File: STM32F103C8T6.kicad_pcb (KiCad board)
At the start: 2 copper layers, 28 parts, among them J1 USB_B_Micro, J2 Conn_01x04_Pin, J3 Conn_01x04_Pin, J4 Conn_01x04_Pin, SW1 SW_SPDT, U1 STM32F103C8T6, U3 AMS1117-3.3, Y1 16MHz

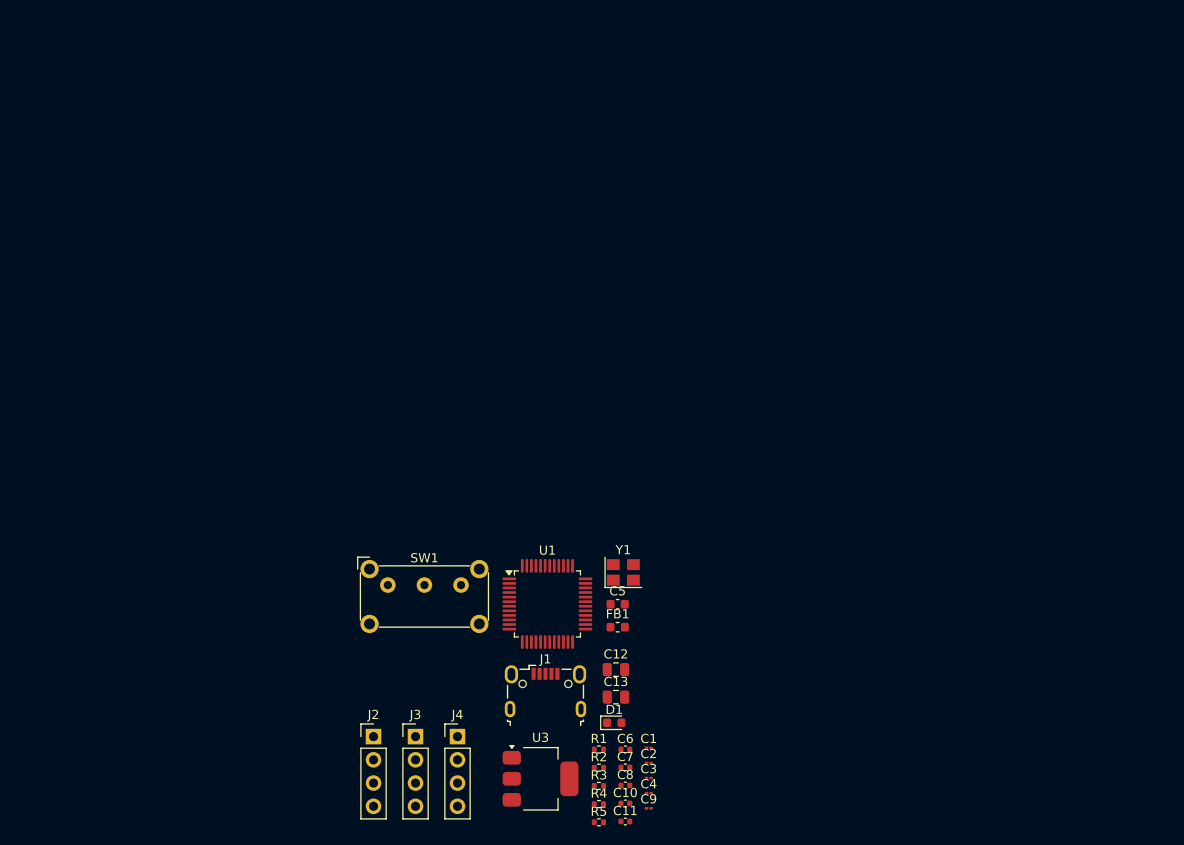
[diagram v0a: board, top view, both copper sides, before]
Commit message: footprint corrected, layout started
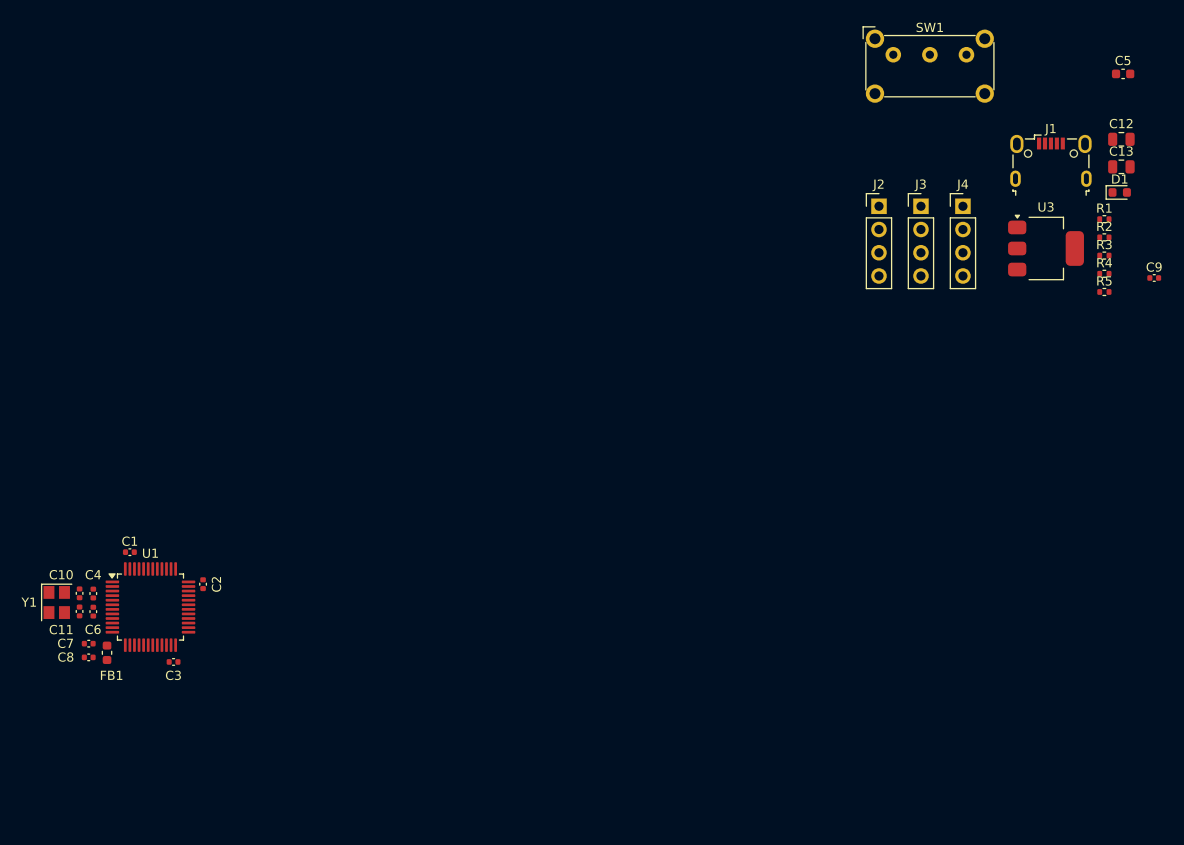
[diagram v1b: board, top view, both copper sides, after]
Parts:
- C1, C2, C3, C4, C9: footprint Capacitor_SMD:C_01005_0402Metric -> Capacitor_SMD:C_0402_1005Metric
- moved C5 80.1 mm to (214.1, 31.7)
- moved SW1 80.1 mm to (189.0, 29.6)
- moved C12 80.1 mm to (213.9, 38.9)
- moved C9 80.1 mm to (217.5, 54.0)
- moved D1 80.1 mm to (213.7, 44.7)
- moved J1 80.1 mm to (206.2, 41.2)
- moved R2 80.1 mm to (212.0, 49.6)
- moved R4 80.1 mm to (212.0, 53.6)
- moved R5 80.1 mm to (212.0, 55.6)
- moved U3 80.1 mm to (205.7, 50.8)
- moved C13 80.1 mm to (213.9, 41.9)
- moved J2 80.1 mm to (187.4, 46.2)
- moved J3 80.1 mm to (192.0, 46.2)
- moved J4 80.1 mm to (196.6, 46.2)
- moved R1 80.1 mm to (212.0, 47.6)
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
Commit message: footprint changes, WIP layout
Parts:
- added H1: MountingHole, MountingHole:MountingHole_2.2mm_M2, F.Cu at (100.0, 100.0)
- added H2: MountingHole, MountingHole:MountingHole_2.2mm_M2, F.Cu at (135.0, 100.0)
- added H3: MountingHole, MountingHole:MountingHole_2.2mm_M2, F.Cu at (135.0, 75.0)
- added H4: MountingHole, MountingHole:MountingHole_2.2mm_M2, F.Cu at (100.0, 75.0)
- SW1: footprint Button_Switch_THT:SW_E-Switch_EG1224_SPDT_Angled -> Button_Switch_SMD:SW_SPDT_PCM12
- moved C5 113.4 mm to (111.2, 79.5)
- moved C9 109.8 mm to (114.2, 91.5)
- moved R1 108.1 mm to (108.3, 78.0)
- moved R5 106.2 mm to (113.3, 94.5), turned to 180 degrees
- moved SW1 104.3 mm to (99.0, 82.5), turned to -90 degrees
- moved R4 103.2 mm to (117.2, 94.5)
- moved C12 102.2 mm to (124.8, 89.0)
- moved C13 100.3 mm to (129.8, 96.5), turned to 90 degrees
- moved J4 98.2 mm to (115.1, 101.0), turned to -90 degrees
- moved D1 95.4 mm to (132.5, 94.8), turned to 90 degrees
- moved U3 93.2 mm to (124.8, 97.0), turned to -90 degrees
- moved R2 92.3 mm to (126.0, 83.0), turned to 90 degrees
- moved J3 90.2 mm to (106.2, 74.0), turned to 90 degrees
- moved R3 88.8 mm to (132.5, 91.0), turned to 90 degrees
- moved J1 83.0 mm to (134.5, 83.0), turned to 90 degrees
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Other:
- board outline added: 42 x 32 mm
